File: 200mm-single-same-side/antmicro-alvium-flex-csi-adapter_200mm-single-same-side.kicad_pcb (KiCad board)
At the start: 2 copper layers, 25.5 x 200.1 mm, 2 parts, among them J1 WE_687622100002_FLEX, J2 WE_687650100002_FLEX

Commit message: 200mm-single-same: update signage
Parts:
- added N1: oshw_logo, antmicro-alvium-flex-csi-adapter-footprints:oshw-logo, B.Cu at (163.5, 232.8)
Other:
- board text added: "Antmicro Alvium Flex CSI Adapter 200mm single same side contacts Rev. 1.0.1"
- board text added: "LED ->"

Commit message: Remove obsolete markings
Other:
- board text removed: "A"

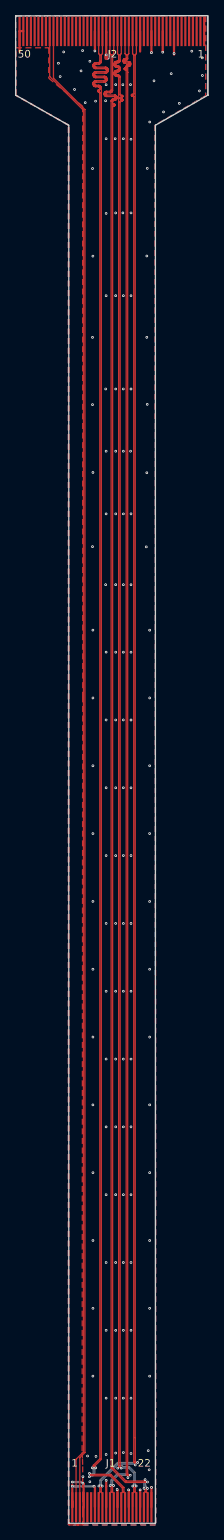
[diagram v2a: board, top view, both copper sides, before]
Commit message: 200mm-single-same: add NMOS transistor for camera triggering
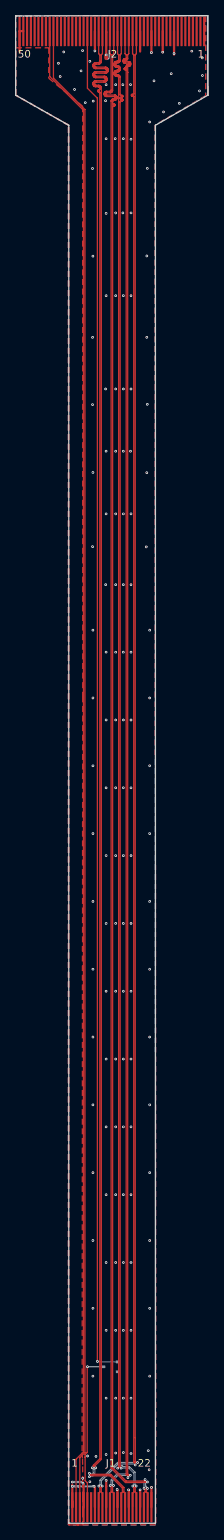
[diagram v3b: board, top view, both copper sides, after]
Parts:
- added Q1: BSS138APW, antmicro-alvium-flex-csi-adapter-footprints:SC70-3, B.Cu at (163.0, 244.0)
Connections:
- J2 pad 32: Net-(J2-Pad32) -> /VSYNC
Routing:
- net /VSYNC: track 0.00 -> 179.8 mm, vias 0 -> 1
- net /GPIO2: track 0.00 -> 21.0 mm, vias 0 -> 1
